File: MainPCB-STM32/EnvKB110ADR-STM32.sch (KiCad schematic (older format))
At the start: 251 parts, among them J1 Conn_01x03, SW1 Boot Mode, SW2 Reset Switch, U1 XC6206PxxxMR, U2 STM32F411CEUx, Y1 3225_4P 32.768khz

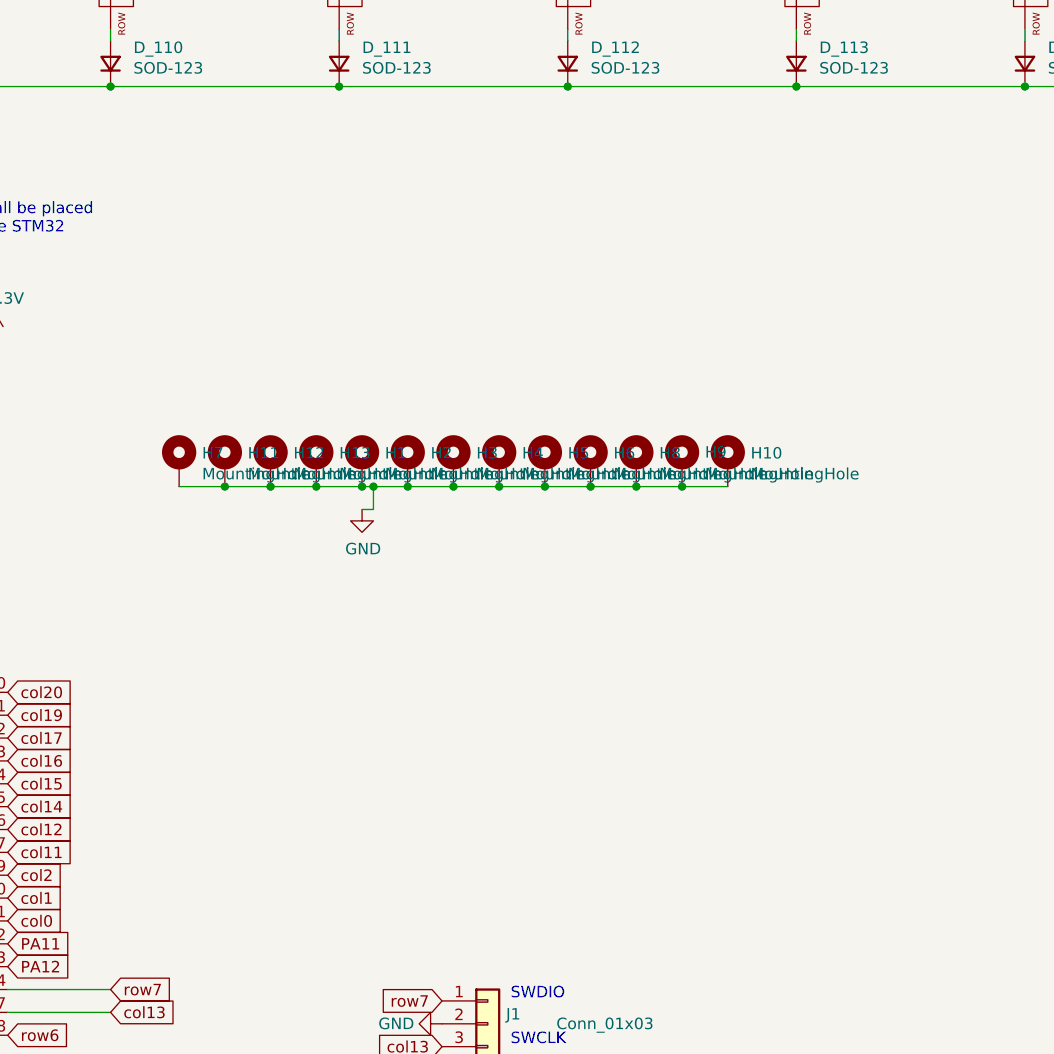
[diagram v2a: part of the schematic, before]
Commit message: general adjustments, fixes and tweaks on STM32 version
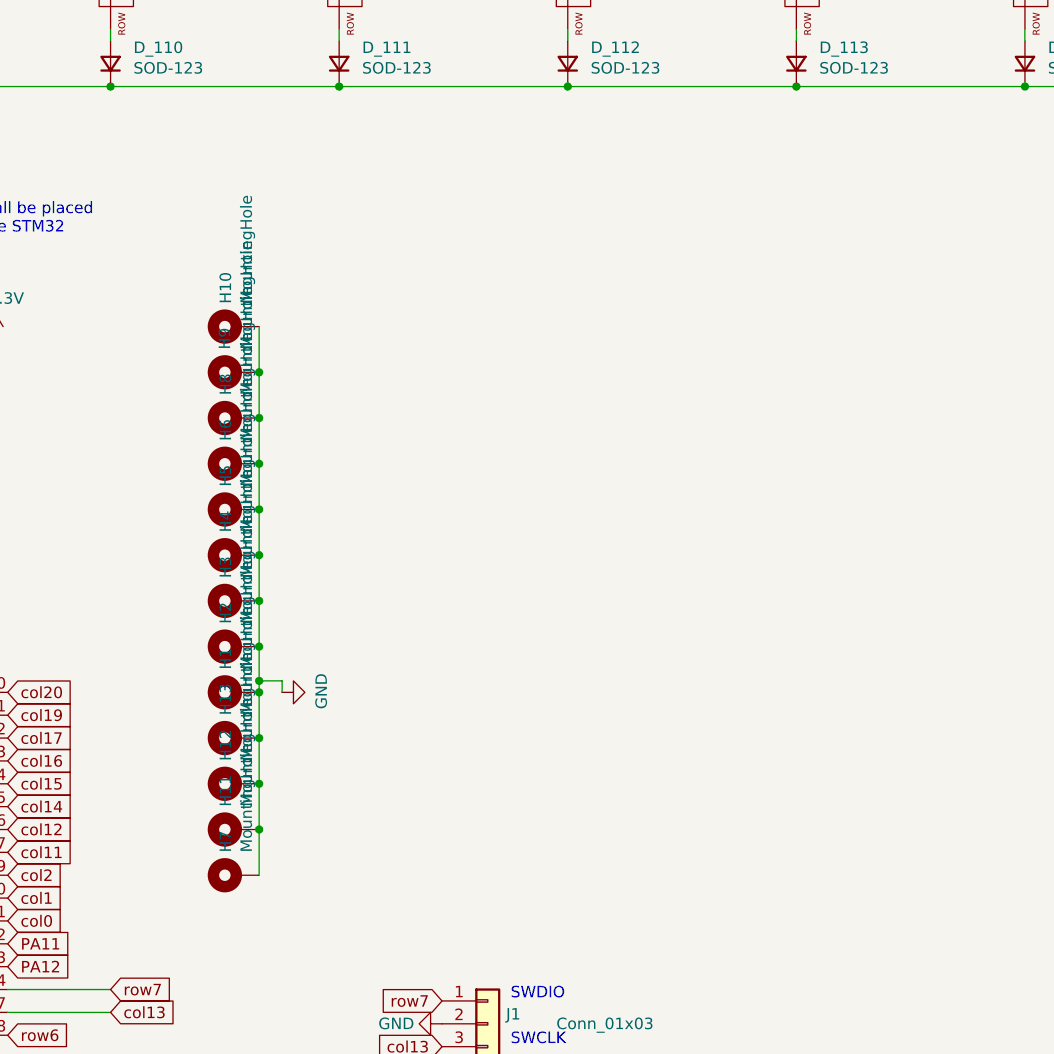
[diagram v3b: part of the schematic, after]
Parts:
- J1: footprint Connector_PinSocket_2.54mm:PinSocket_1x03_P2.54mm_Horizontal -> Connector_PinSocket_2.54mm:PinSocket_1x03_P2.54mm_Vertical
- K_100, K_101, K_102, K_112, K_113, K_114, K_116, K_12, K_13, K_14, K_15, K_16, K_17, K_18, K_19, K_20, K_21, K_22, K_23, K_24, K_25, K_26, K_27, K_28, K_29, K_30, K_31, K_32, K_33, K_34, K_35, K_36, K_37, K_38, K_39, K_40, K_42, K_43, K_44, K_45, K_46, K_47, K_48, K_50, K_51, K_52, K_53, K_54, K_55, K_56, K_57, K_58, K_59, K_60, K_61, K_63, K_64, K_65, K_66, K_67, K_68, K_71, K_72, K_73, K_74, K_75, K_76, K_77, K_78, K_79, K_80, K_81, K_82, K_83, K_84, K_85, K_87, K_88, K_89, K_90, K_91, K_92, K_93, K_94, K_95, K_96, K_97, K_99: footprint MX_Only:MXOnly-1U-Hotswap -> MX_Only:MXOnly-1U-Hotswap-custom
- K_103, K_115, K_41, K_62, K_69: footprint MX_Only:MXOnly-2U-Hotswap -> MX_Only:MXOnly-1U-Hotswap-custom
- K_104, K_105, K_106, K_108, K_109, K_110, K_111, K_86: footprint MX_Only:MXOnly-1.25U-Hotswap -> MX_Only:MXOnly-1U-Hotswap-custom
- K_107: footprint MX_Only:MXOnly-6.25U-Hotswap-ReversedStabilizers -> MX_Only:MXOnly-1U-Hotswap-custom
- K_49, K_ANSI_3: footprint MX_Only:MXOnly-1.5U-Hotswap -> MX_Only:MXOnly-1U-Hotswap-custom
- K_70: footprint MX_Only:MXOnly-1.75U-Hotswap -> MX_Only:MXOnly-1U-Hotswap-custom
- K_98: footprint MX_Only:MXOnly-2.75U-Hotswap -> MX_Only:MXOnly-1U-Hotswap-custom
- K_ANSI_1, K_ANSI_2: footprint MX_Only:MXOnly-2.25U-Hotswap -> MX_Only:MXOnly-1U-Hotswap-custom
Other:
- moved on the sheet: H1, H10, H11, H12, H13, H2, H3, H4, H5, H6, H7, H8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

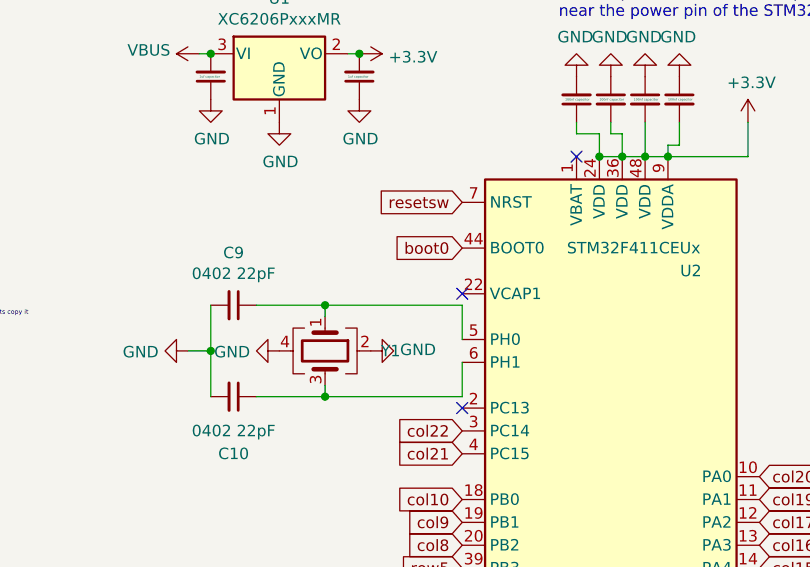
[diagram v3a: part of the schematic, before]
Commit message: added missing capacitor on vcap
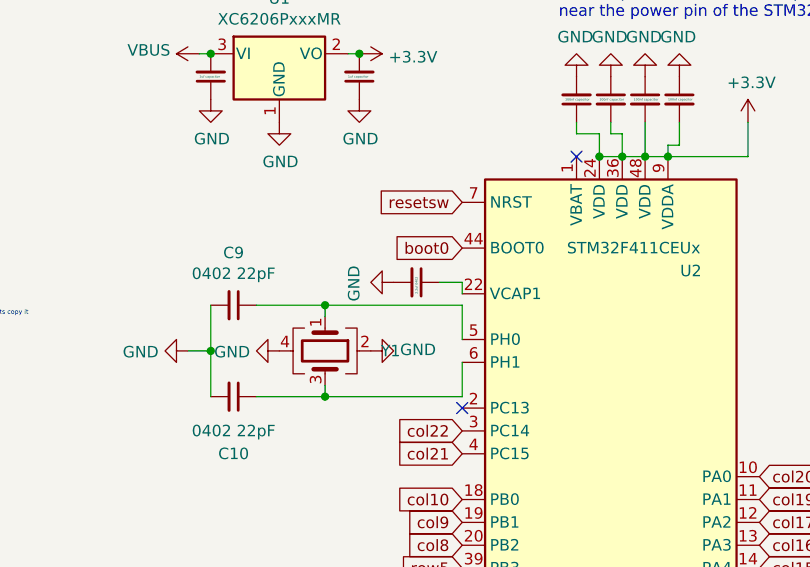
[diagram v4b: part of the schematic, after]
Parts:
- added C11: 2.2uf 0402, Capacitor_SMD:C_0402_1005Metric, symbol Device:C_Small
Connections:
- net GND: now also C11.2
- net at U2.22 (VCAP1): now also C11.1
- no-connect marks 5 -> 4
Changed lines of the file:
@@
 	13400 12950 13500 12950
 NoConn ~ 13200 9850
-NoConn ~ 12700 10450
 $Comp
 L Device:Crystal_GND24 Y1
@@
 Wire Wire Line
 	15100 11450 15100 11250
+$Comp
+L power:GND #PWR0122
+U 1 1 61AA5782
+P 12400 10400
+F 0 "#PWR0122" H 12400 10150 50  0001 C CNN
+F 1 "GND" H 12405 10227 50  0000 C CNN
+F 2 "" H 12400 10400 50  0001 C CNN
+F 3 "" H 12400 10400 50  0001 C CNN
+	1    12400 10400
+	0    1    1    0
+$EndComp
+$Comp
+L Device:C_Small C11
+U 1 1 61AA6CDC
+P 12500 10400
+F 0 "C11" H 12592 10446 50  0001 L CNN
+F 1 "2.2uf 0402" H 12450 10400 10  0000 L CNN
+F 2 "Capacitor_SMD:C_0402_1005Metric" H 12500 10400 50  0001 C CNN
+F 3 "~" H 12500 10400 50  0001 C CNN
+	1    12500 10400
+	0    1    -1   0
+$EndComp
+Wire Wire Line
+	12600 10400 12700 10400
+Wire Wire Line
+	12700 10400 12700 10450
 $EndSCHEMATC

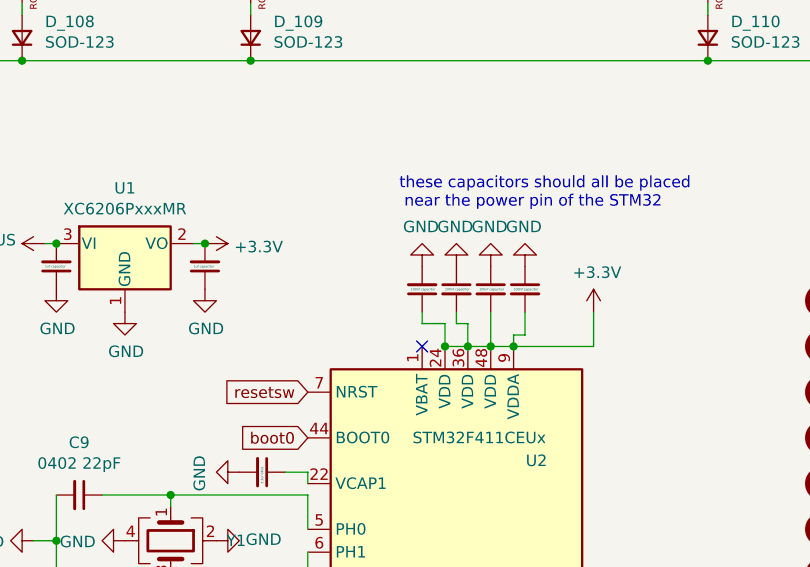
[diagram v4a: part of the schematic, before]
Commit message: added missing capacitor and power connection
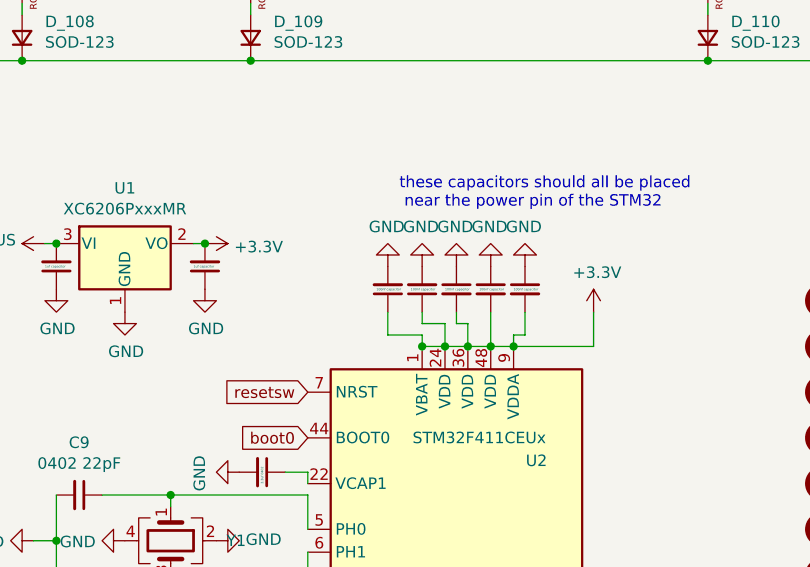
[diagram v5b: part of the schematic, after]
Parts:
- added C12: 100nf capacitor, Capacitor_SMD:C_0402_1005Metric, symbol Device:C_Small
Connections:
- net +3V3: now also U2.1 (VBAT), C12.1
- net GND: now also C12.2
- no-connect marks 4 -> 3
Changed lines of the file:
@@
-$EndComp
-$Comp
-L MCU_ST_STM32F4:STM32F411CEUx U2
-U 1 1 61118AF8
-P 13400 11350
-F 0 "U2" H 13700 12350 50  0000 C CNN
-F 1 "STM32F411CEUx" H 13450 12450 50  0000 C CNN
-F 2 "Package_DFN_QFN:QFN-48-1EP_7x7mm_P0.5mm_EP5.6x5.6mm" H 12800 9850 50  0001 R CNN
-F 3 "http://www.st.com/st-web-ui/static/active/en/resource/technical/document/datasheet/DM00115249.pdf" H 13400 11350 50  0001 C CNN
-	1    13400 11350
-	1    0    0    -1
 $EndComp
 $Comp
@@
 row7
 Wire Wire Line
-	13500 12950 13600 12950
-Wire Wire Line
 	13500 9700 13500 9850
-Connection ~ 13300 9850
-Connection ~ 13600 12950
 Connection ~ 15450 6600
 Wire Wire Line
@@
 Wire Wire Line
 	1900 2150 1900 4150
-Connection ~ 13500 12950
-Wire Wire Line
-	13200 12950 13300 12950
-Connection ~ 13300 12950
-Wire Wire Line
-	13300 12950 13400 12950
-Connection ~ 13400 12950
-Wire Wire Line
-	13400 12950 13500 12950
-NoConn ~ 13200 9850
 $Comp
 L Device:Crystal_GND24 Y1
@@
 Wire Wire Line
 	12700 10400 12700 10450
+Connection ~ 13600 12950
+Wire Wire Line
+	13500 12950 13600 12950
+Connection ~ 13500 12950
+Wire Wire Line
+	13400 12950 13500 12950
+Connection ~ 13400 12950
+Wire Wire Line
+	13300 12950 13400 12950
+Wire Wire Line
+	13200 12950 13300 12950
+Connection ~ 13300 12950
+Connection ~ 13300 9850
+$Comp
+L MCU_ST_STM32F4:STM32F411CEUx U2
+U 1 1 61118AF8
+P 13400 11350
+F 0 "U2" H 13700 12350 50  0000 C CNN
+F 1 "STM32F411CEUx" H 13450 12450 50  0000 C CNN
+F 2 "Package_DFN_QFN:QFN-48-1EP_7x7mm_P0.5mm_EP5.6x5.6mm" H 12800 9850 50  0001 R CNN
+F 3 "http://www.st.com/st-web-ui/static/active/en/resource/technical/document/datasheet/DM00115249.pdf" H 13400 11350 50  0001 C CNN
+	1    13400 11350
+	1    0    0    -1
+$EndComp
+Wire Wire Line
+	13200 9850 13300 9850
+$Comp
+L power:GND #PWR0123
+U 1 1 61AEBF37
+P 13050 9500
+F 0 "#PWR0123" H 13050 9250 50  0001 C CNN
+F 1 "GND" H 13055 9327 50  0000 C CNN
+F 2 "" H 13050 9500 50  0001 C CNN
+F 3 "" H 13050 9500 50  0001 C CNN
+	1    13050 9500
+	-1   0    0    1
+$EndComp
+$Comp
+L Device:C_Small C12
+U 1 1 61AED4AD
+P 13050 9600
+F 0 "C12" H 13142 9646 50  0001 L CNN
+F 1 "100nf capacitor" H 13000 9600 10  0000 L CNN
+F 2 "Capacitor_SMD:C_0402_1005Metric" H 13050 9600 50  0001 C CNN
+F 3 "~" H 13050 9600 50  0001 C CNN
+	1    13050 9600
+	1    0    0    1
+$EndComp
+Wire Wire Line
+	13050 9700 13050 9800
+Connection ~ 13200 9850
+Wire Wire Line
+	13200 9850 13200 9800
+Wire Wire Line
+	13200 9800 13050 9800
 $EndSCHEMATC
